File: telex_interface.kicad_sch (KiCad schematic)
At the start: 58 parts, among them J1 DB25_Female_MountingHoles, J2 Conn_02x20_Odd_Even, J3 Conn_01x03_Male, J4 Conn_02x04_Odd_Even, U1 max3387, U2 74LVC1G08

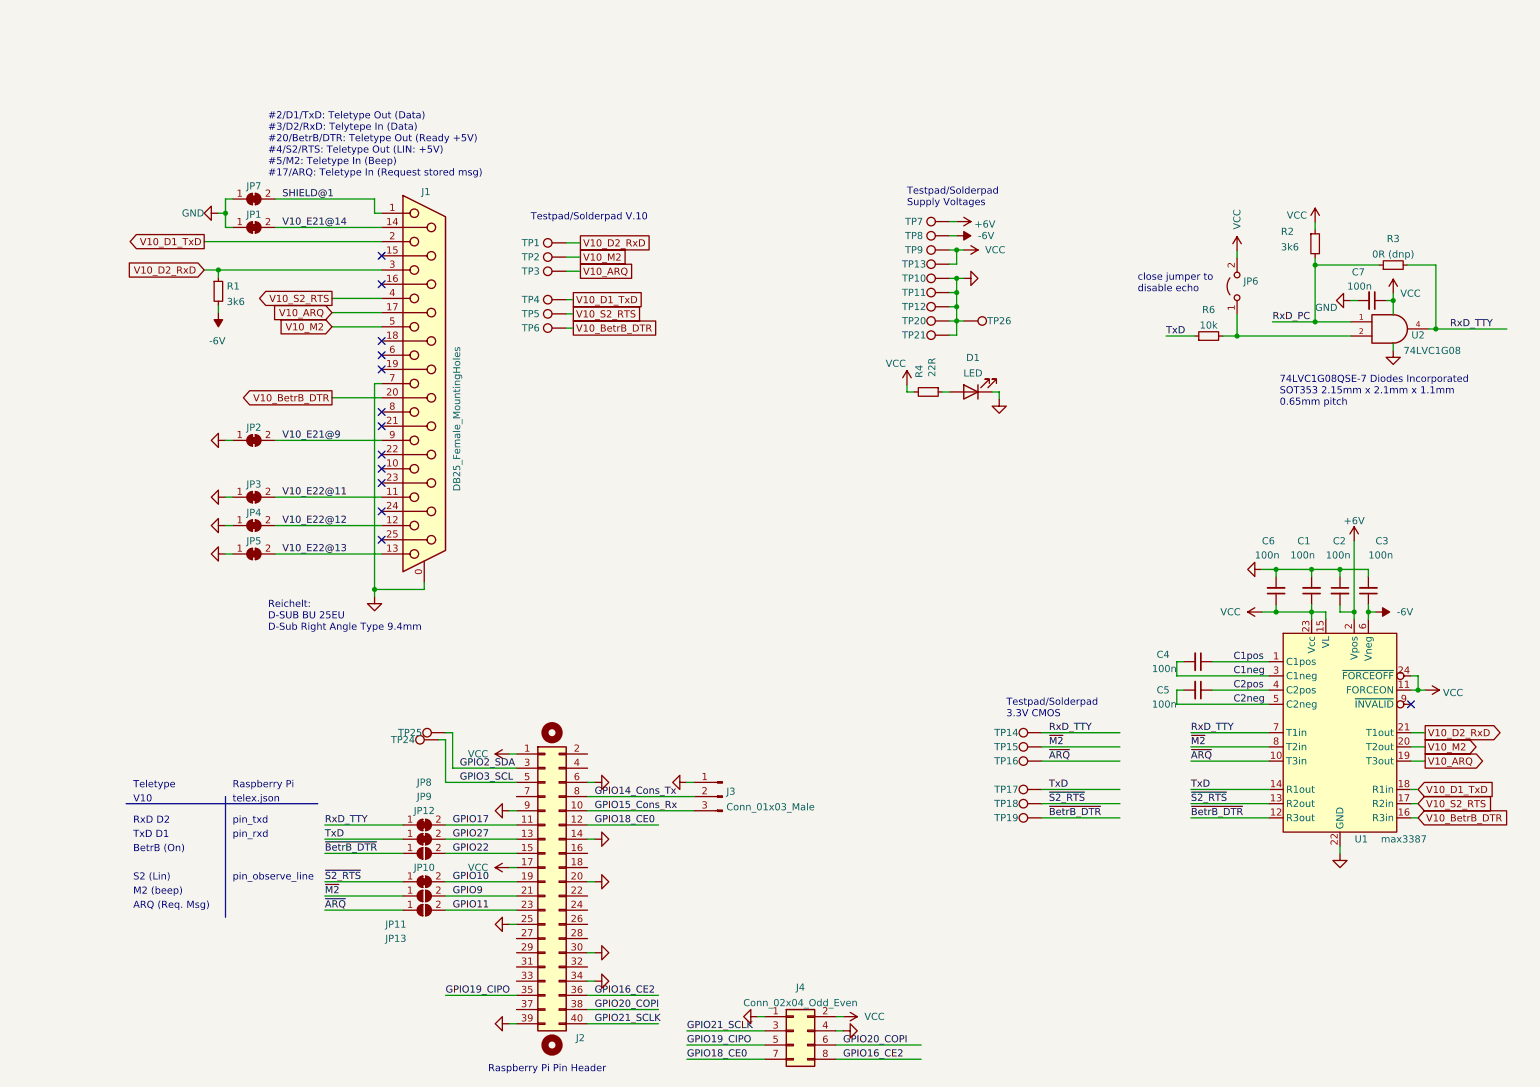
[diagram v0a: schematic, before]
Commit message: Remove _ from labels.
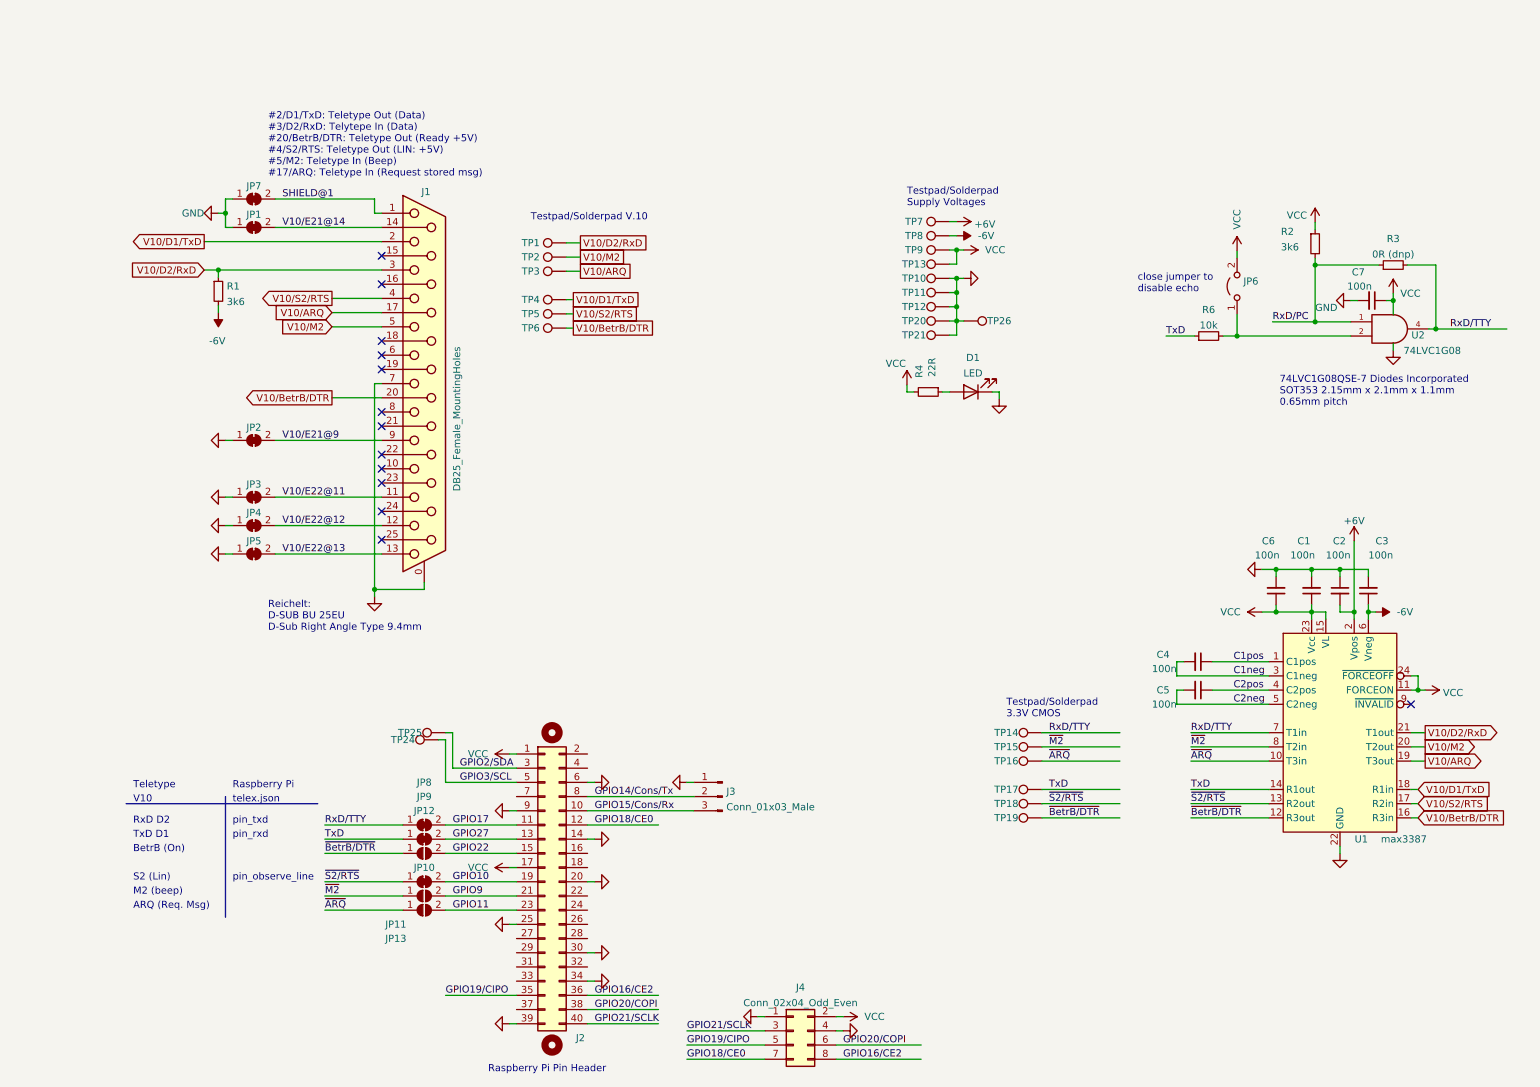
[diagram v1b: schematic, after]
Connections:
- net GPIO14_Cons_Tx renamed GPIO14/Cons/Tx
- net GPIO15_Cons_Rx renamed GPIO15/Cons/Rx
- net GPIO16_CE2 renamed GPIO16/CE2
- net GPIO18_CE0 renamed GPIO18/CE0
- net GPIO19_CIPO renamed GPIO19/CIPO
- net GPIO20_COPI renamed GPIO20/COPI
- net GPIO21_SCLK renamed GPIO21/SCLK
- net GPIO2_SDA renamed GPIO2/SDA
- net GPIO3_SCL renamed GPIO3/SCL
- net RxD_PC renamed RxD/PC
- net RxD_TTY renamed RxD/TTY
- net V10_ARQ renamed V10/ARQ
- net V10_BetrB_DTR renamed V10/BetrB/DTR
- net V10_D1_TxD renamed V10/D1/TxD
- net V10_D2_RxD renamed V10/D2/RxD
- net V10_E21@14 renamed V10/E21@14
- net V10_E21@9 renamed V10/E21@9
- net V10_E22@11 renamed V10/E22@11
- net V10_E22@12 renamed V10/E22@12
- net V10_E22@13 renamed V10/E22@13
- net V10_M2 renamed V10/M2
- net V10_S2_RTS renamed V10/S2/RTS
- net ~{BetrB_DTR} renamed ~{BetrB/DTR}
- net ~{S2_RTS} renamed ~{S2/RTS}

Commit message: Changes needed for kicad 5.99 - 6.99
Fix alignment issue in schematic.
Newly introduced warning about silkscreen width/text height:
 - change design rules to match what was already successfully produced

Because of rounding issues (I guess, moving traces by 1 pixel or so
makes DRC pass) I turned off "soldermask aperture over traces with
different nets".
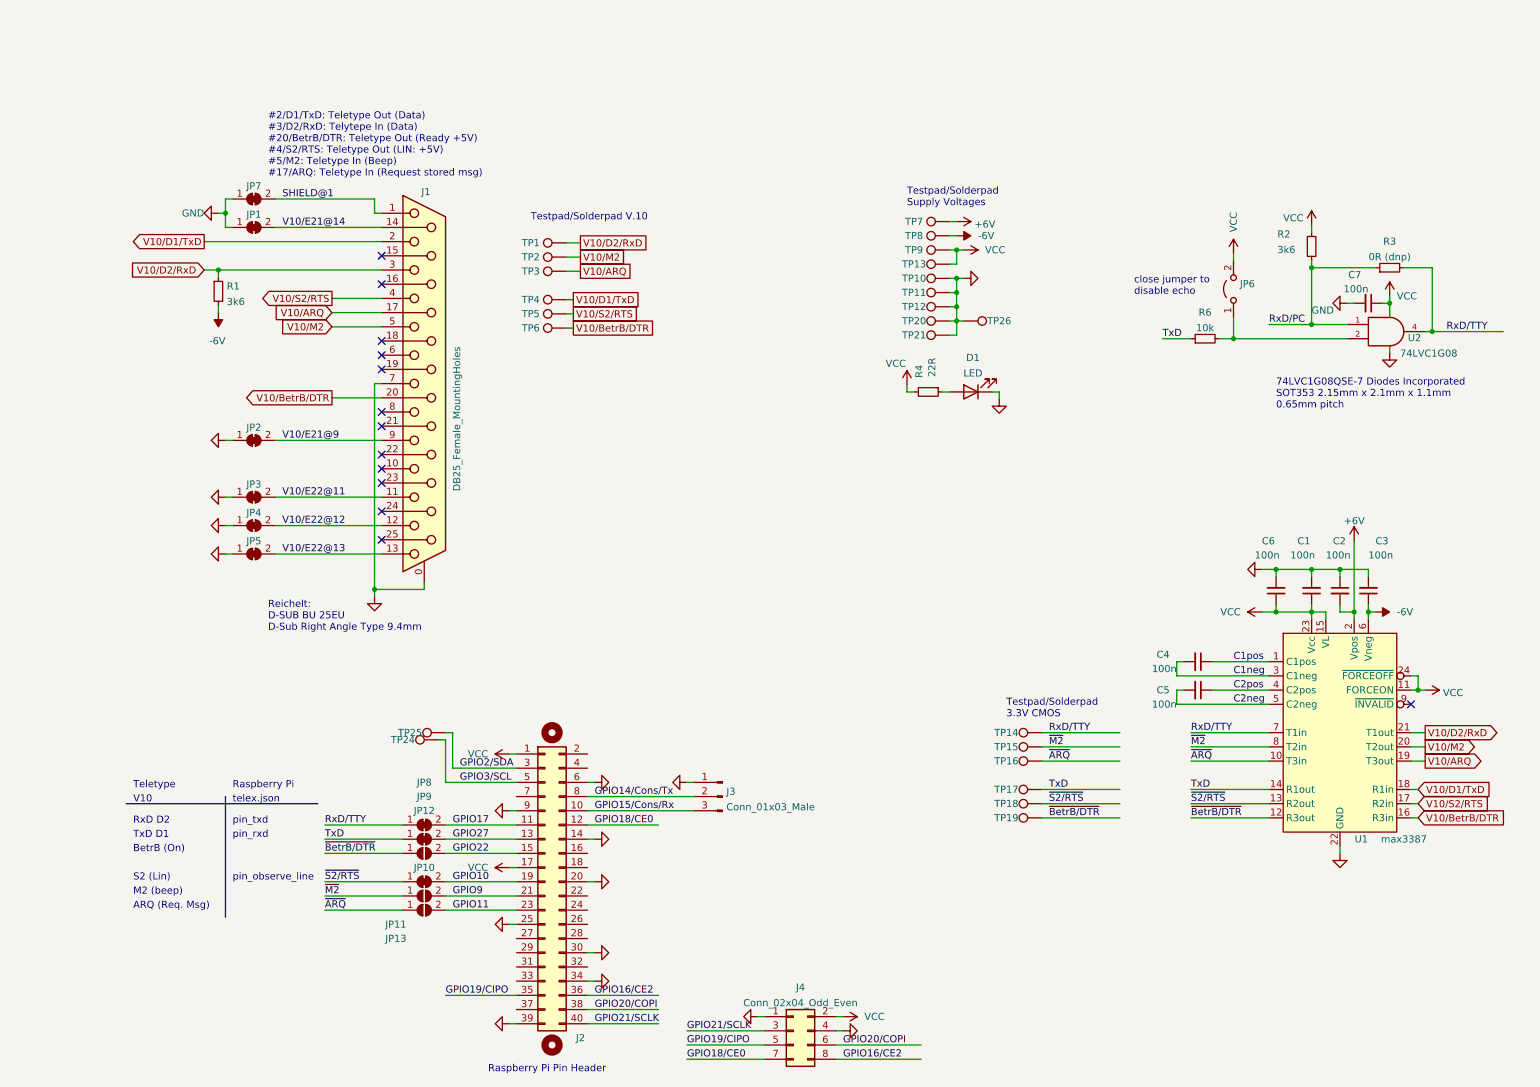
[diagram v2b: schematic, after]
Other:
- moved on the sheet: C7, JP6, R2, R3, R6, U2

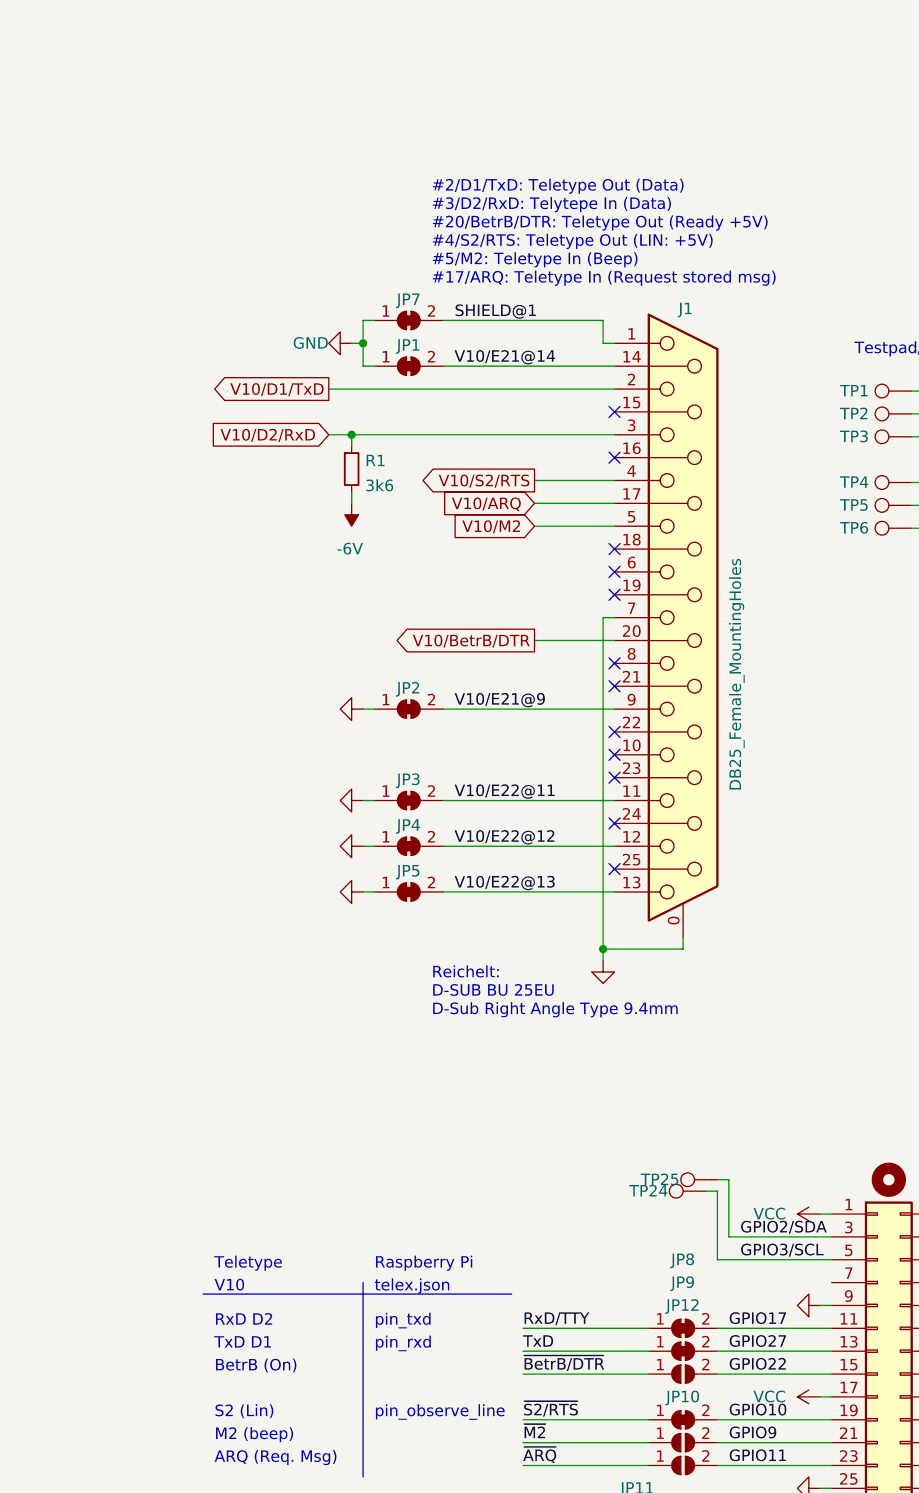
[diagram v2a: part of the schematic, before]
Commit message: Fix mistakes made during first spin of board (RevA):
R1 Pulldown to -6V was on RxD (input of TTY, output of maxim driver)
instead of TxD (output of TTY, input of maxim driver).
  ==> moved to V10/D1/TxD signal, Pin 2 of DSUB

Raspi GPIO17 was on net RxD/TTY (output of the single gate buffer U2)
instead of net RxD/PC (input to U2), so both outputs (raspi & U2) were
on the same net.
  ==> connected GPIO17 to net RxD/PC

Silkscreen: RxD/TxD labels were swapped near JP8/JP9 on the bottom
of the PCB, adding even more confusion ;).
  ==> Fixed silkscreen labels.
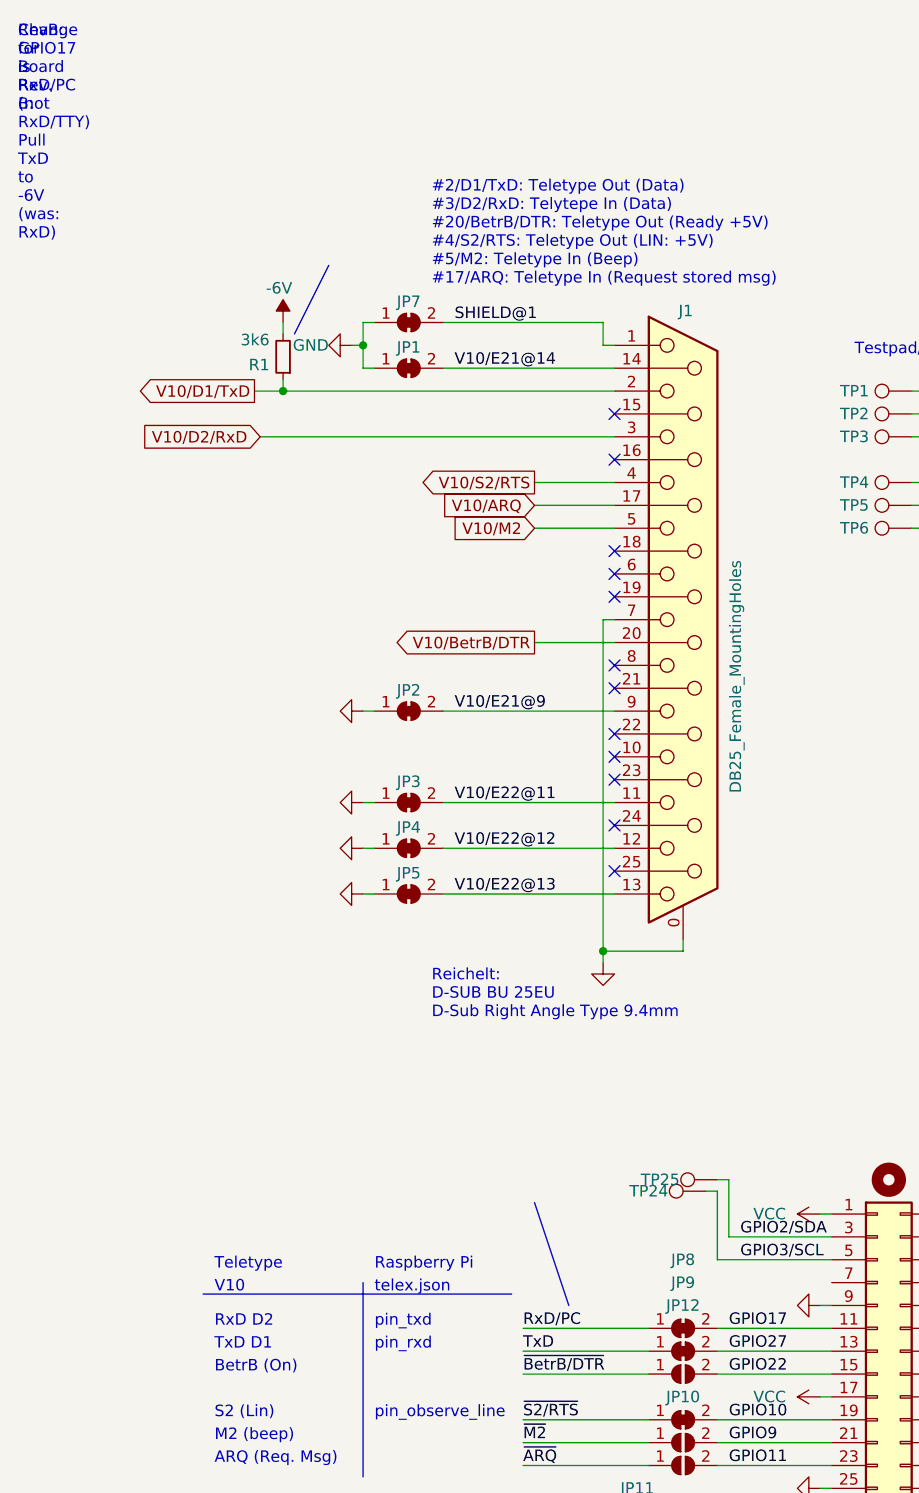
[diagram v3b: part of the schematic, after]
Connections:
- net RxD/TTY: no longer JP8.1 (A)
- net V10/D1/TxD: now also R1.1
- net V10/D2/RxD: no longer R1.1
- new net RxD/PC: JP8.1 (A)
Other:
- moved on the sheet: R1
